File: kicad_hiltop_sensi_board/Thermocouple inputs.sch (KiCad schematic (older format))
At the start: 28 parts, among them U23 MAX4194, U24 MAX4194, U25 MAX4194, U26 MAX4194

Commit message: Updated board layout LBBC sensi board
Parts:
- R69: value R -> 100R 0.1%
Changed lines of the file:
@@
 	0    1    1    0
-$EndComp
-$Comp
-L Devtank:+3.3V #PWR0134
-U 1 1 5DE2BF89
-P 4500 1450
-F 0 "#PWR0134" H 4500 1300 50  0001 C CNN
-F 1 "+3.3V" H 4515 1623 50  0000 C CNN
-F 2 "" H 4500 1450 50  0000 C CNN
-F 3 "" H 4500 1450 50  0000 C CNN
-	1    4500 1450
-	1    0    0    -1
 $EndComp
 Connection ~ 4500 2600
@@
 	0    1    1    0
 $EndComp
-$Comp
-L Devtank:+3.3V #PWR0153
-U 1 1 5D86DCA3
-P 8300 1450
-F 0 "#PWR0153" H 8300 1300 50  0001 C CNN
-F 1 "+3.3V" H 8315 1623 50  0000 C CNN
-F 2 "" H 8300 1450 50  0000 C CNN
-F 3 "" H 8300 1450 50  0000 C CNN
-	1    8300 1450
-	1    0    0    -1
-$EndComp
 Connection ~ 8300 2600
 Wire Wire Line
@@
 	0    1    1    0
 $EndComp
-$Comp
-L Devtank:+3.3V #PWR0168
-U 1 1 5D874544
-P 4500 3850
-F 0 "#PWR0168" H 4500 3700 50  0001 C CNN
-F 1 "+3.3V" H 4515 4023 50  0000 C CNN
-F 2 "" H 4500 3850 50  0000 C CNN
-F 3 "" H 4500 3850 50  0000 C CNN
-	1    4500 3850
-	1    0    0    -1
-$EndComp
 Connection ~ 4500 5000
 Wire Wire Line
@@
 P 3850 4600
 F 0 "R69" H 3920 4646 50  0000 L CNN
-F 1 "R" H 3920 4555 50  0000 L CNN
+F 1 "100R 0.1%" H 3650 4450 50  0000 L CNN
 F 2 "Resistor_SMD:R_0603_1608Metric" V 3780 4600 50  0001 C CNN
 F 3 "" H 3850 4600 50  0001 C CNN
@@
 	0    1    1    0
 $EndComp
-$Comp
-L Devtank:+3.3V #PWR0173
-U 1 1 5D879C85
-P 8250 3800
-F 0 "#PWR0173" H 8250 3650 50  0001 C CNN
-F 1 "+3.3V" H 8265 3973 50  0000 C CNN
-F 2 "" H 8250 3800 50  0000 C CNN
-F 3 "" H 8250 3800 50  0000 C CNN
-	1    8250 3800
-	1    0    0    -1
-$EndComp
 Connection ~ 8250 4950
 Wire Wire Line
@@
 Wire Wire Line
 	6700 4750 7150 4750
+$Comp
+L power:+3V3 #PWR?
+U 1 1 5E6F1DC0
+P 4500 1450
+AR Path="/5E6F1DC0" Ref="#PWR?"  Part="1"
+AR Path="/5D6F87E7/5E6F1DC0" Ref="#PWR0247"  Part="1"
+F 0 "#PWR0247" H 4500 1300 50  0001 C CNN
+F 1 "+3V3" H 4515 1623 50  0000 C CNN
+F 2 "" H 4500 1450 50  0001 C CNN
+F 3 "" H 4500 1450 50  0001 C CNN
+	1    4500 1450
+	1    0    0    -1
+$EndComp
+$Comp
+L power:+3V3 #PWR?
+U 1 1 5E6F9A9C
+P 8300 1450
+AR Path="/5E6F9A9C" Ref="#PWR?"  Part="1"
+AR Path="/5D6F87E7/5E6F9A9C" Ref="#PWR0251"  Part="1"
+F 0 "#PWR0251" H 8300 1300 50  0001 C CNN
+F 1 "+3V3" H 8315 1623 50  0000 C CNN
+F 2 "" H 8300 1450 50  0001 C CNN
+F 3 "" H 8300 1450 50  0001 C CNN
+	1    8300 1450
+	1    0    0    -1
+$EndComp
+$Comp
+L power:+3V3 #PWR?
+U 1 1 5E702ADB
+P 4500 3850
+AR Path="/5E702ADB" Ref="#PWR?"  Part="1"
+AR Path="/5D6F87E7/5E702ADB" Ref="#PWR0259"  Part="1"
+F 0 "#PWR0259" H 4500 3700 50  0001 C CNN
+F 1 "+3V3" H 4515 4023 50  0000 C CNN
+F 2 "" H 4500 3850 50  0001 C CNN
+F 3 "" H 4500 3850 50  0001 C CNN
+	1    4500 3850
+	1    0    0    -1
+$EndComp
+$Comp
+L power:+3V3 #PWR?
+U 1 1 5E70B2B1
+P 8250 3800
+AR Path="/5E70B2B1" Ref="#PWR?"  Part="1"
+AR Path="/5D6F87E7/5E70B2B1" Ref="#PWR0260"  Part="1"
+F 0 "#PWR0260" H 8250 3650 50  0001 C CNN
+F 1 "+3V3" H 8265 3973 50  0000 C CNN
+F 2 "" H 8250 3800 50  0001 C CNN
+F 3 "" H 8250 3800 50  0001 C CNN
+	1    8250 3800
+	1    0    0    -1
+$EndComp
 $EndSCHEMATC

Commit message: Sensi board updated pin map
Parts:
- C68, C69, C86, C87: footprint Capacitor_SMD:C_0603_1608Metric -> Capacitor_SMD:C_0402_1005Metric
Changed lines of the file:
@@
 F 0 "C68" V 4548 1800 50  0000 C CNN
 F 1 "0.1uF" V 4639 1800 50  0000 C CNN
-F 2 "Capacitor_SMD:C_0603_1608Metric" H 4838 1650 50  0001 C CNN
+F 2 "Capacitor_SMD:C_0402_1005Metric" H 4838 1650 50  0001 C CNN
 F 3 "" H 4800 1800 50  0001 C CNN
 	1    4800 1800
@@
 F 0 "C87" V 8348 1800 50  0000 C CNN
 F 1 "0.1uF" V 8439 1800 50  0000 C CNN
-F 2 "Capacitor_SMD:C_0603_1608Metric" H 8638 1650 50  0001 C CNN
+F 2 "Capacitor_SMD:C_0402_1005Metric" H 8638 1650 50  0001 C CNN
 F 3 "" H 8600 1800 50  0001 C CNN
 	1    8600 1800
@@
 F 0 "C69" V 4548 4200 50  0000 C CNN
 F 1 "0.1uF" V 4639 4200 50  0000 C CNN
-F 2 "Capacitor_SMD:C_0603_1608Metric" H 4838 4050 50  0001 C CNN
+F 2 "Capacitor_SMD:C_0402_1005Metric" H 4838 4050 50  0001 C CNN
 F 3 "" H 4800 4200 50  0001 C CNN
 	1    4800 4200
@@
 F 0 "C86" V 8298 4150 50  0000 C CNN
 F 1 "0.1uF" V 8389 4150 50  0000 C CNN
-F 2 "Capacitor_SMD:C_0603_1608Metric" H 8588 4000 50  0001 C CNN
+F 2 "Capacitor_SMD:C_0402_1005Metric" H 8588 4000 50  0001 C CNN
 F 3 "" H 8550 4150 50  0001 C CNN
 	1    8550 4150

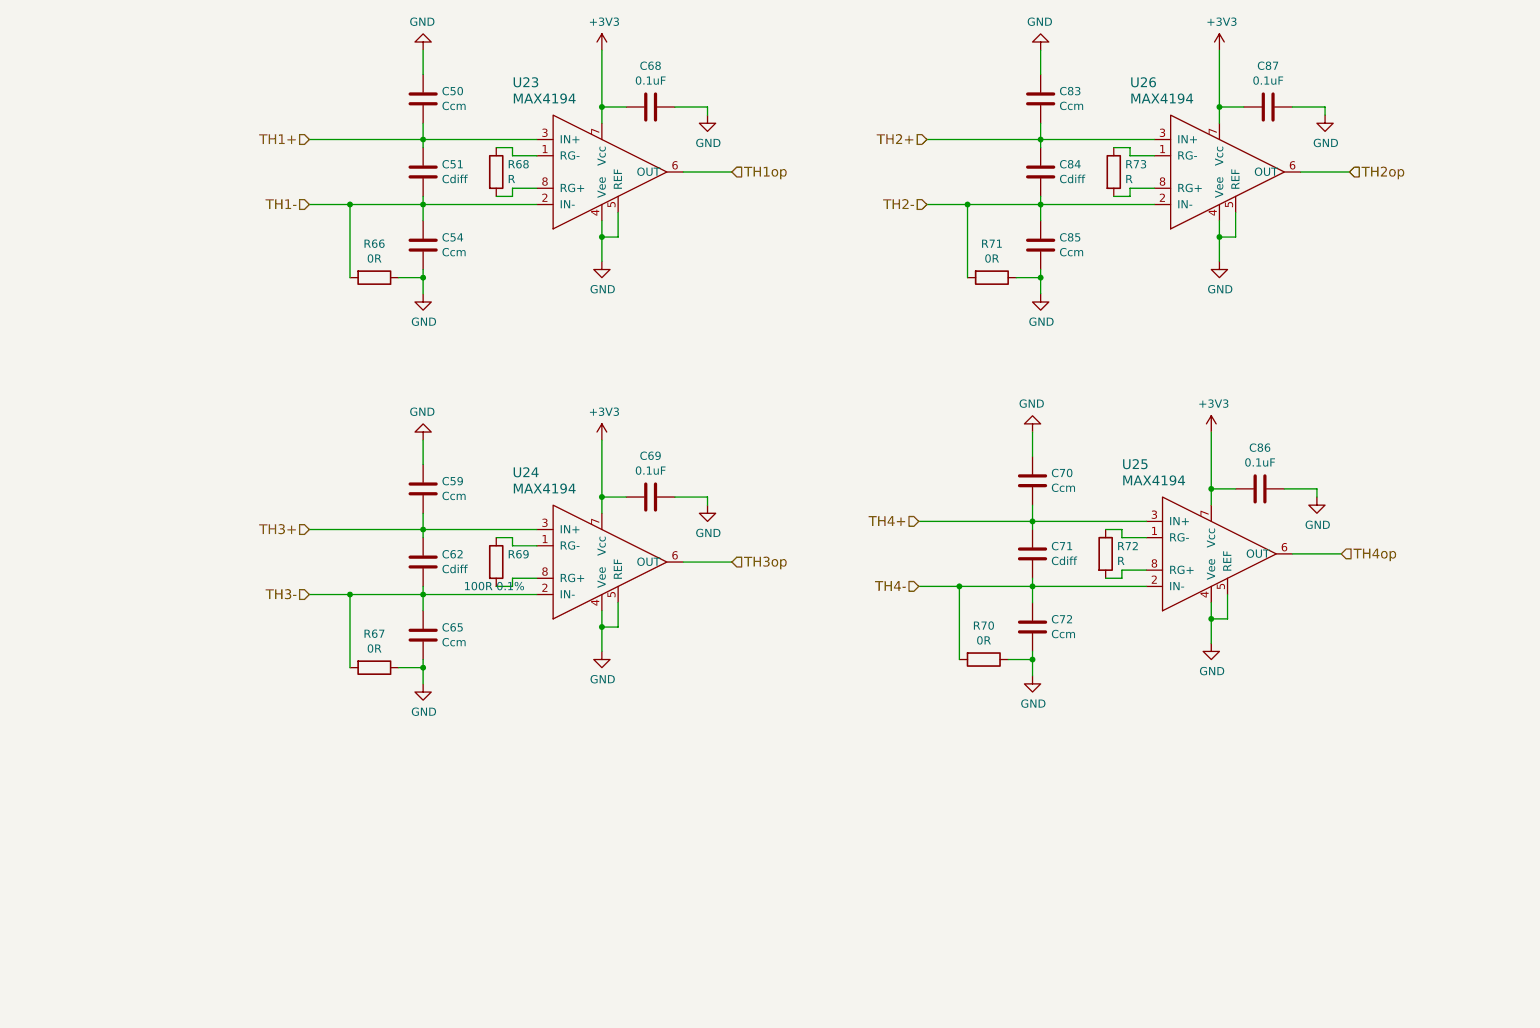
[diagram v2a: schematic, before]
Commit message: Updated sensi board pin map and layout before PCB tracking
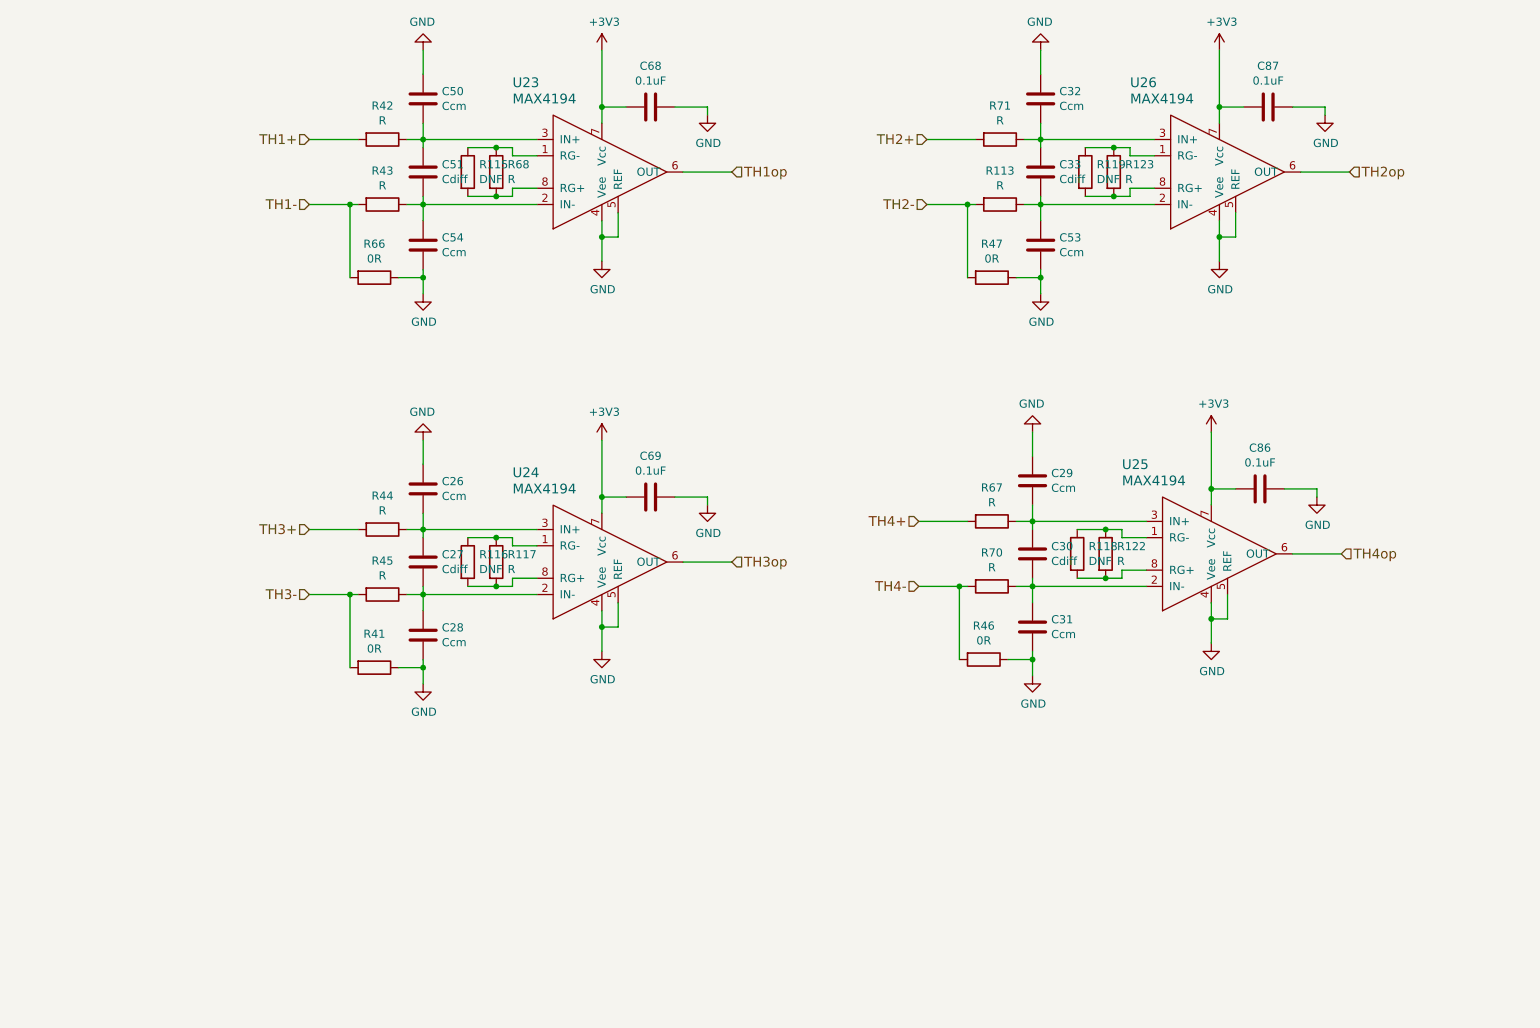
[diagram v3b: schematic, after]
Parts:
- removed C59, C65, C70, C72, C83, C85: Ccm, Capacitor_SMD:C_0603_1608Metric, symbol device:C
- removed C62, C71, C84: Cdiff, Capacitor_SMD:C_0603_1608Metric, symbol device:C
- removed R69: 100R 0.1%, Resistor_SMD:R_0603_1608Metric, symbol device:R
- removed R72, R73: R, Resistor_SMD:R_0603_1608Metric, symbol device:R
- added C26, C28, C29, C31, C32, C53: Ccm, Capacitor_SMD:C_0603_1608Metric, symbol device:C
- added C27, C30, C33: Cdiff, Capacitor_SMD:C_0603_1608Metric, symbol device:C
- added R113, R117, R122, R123, R42, R43, R44, R45: R, Resistor_SMD:R_0603_1608Metric, symbol device:R
- added R115, R116, R118, R119: DNF, Resistor_SMD:R_0603_1608Metric, symbol device:R
- added R41, R46, R47: 0R, Resistor_SMD:R_0603_1608Metric, symbol device:R
- C68, C69, C86, C87: Devtank (none) -> 105-019
- R66: Devtank (none) -> 101-005
- R67, R70, R71: value 0R -> R
- R68: Tolerance (none) -> 0.1%
- U23, U24, U25, U26: Devtank (none) -> 120-005
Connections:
- net GND: now also C26.1, C28.2, C29.1, C31.2, C32.1, C53.2, R41.1, R46.1, R47.1; no longer R67.1, R70.1, R71.1
- net TH1+: now also R42.2; no longer C50.2, C51.1, U23.3 (IN+)
- net TH1-: now also R43.2; no longer C51.2, C54.1, U23.2 (IN-)
- net TH2+: now also R71.2; no longer U26.3 (IN+)
- net TH2-: now also R113.2, R47.2; no longer R71.2, U26.2 (IN-)
- net TH3+: now also R44.2; no longer U24.3 (IN+)
- net TH3-: now also R41.2, R45.2; no longer R67.2, U24.2 (IN-)
- net TH4+: now also R67.2; no longer U25.3 (IN+)
- net TH4-: now also R46.2; no longer U25.2 (IN-)
- net at R68.1, U23.1 (RG-): now also R115.1
- net at R68.2, U23.8 (RG+): now also R115.2
- net at U26.1 (RG-): now also R119.1, R123.1
- net at U26.8 (RG+): now also R119.2, R123.2
- net at U24.1 (RG-): now also R116.1, R117.1
- net at U24.8 (RG+): now also R116.2, R117.2
- net at U25.1 (RG-): now also R118.1, R122.1
- net at U25.8 (RG+): now also R118.2, R122.2
- new net: C51.2, C54.1, R43.1, U23.2 (IN-)
- new net: C50.2, C51.1, R42.1, U23.3 (IN+)
- new net: C33.2, C53.1, R113.1, U26.2 (IN-)
- new net: C32.2, C33.1, R71.1, U26.3 (IN+)
- new net: C27.2, C28.1, R45.1, U24.2 (IN-)
- new net: C26.2, C27.1, R44.1, U24.3 (IN+)
- new net: C30.2, C31.1, R70.1, U25.2 (IN-)
- new net: C29.2, C30.1, R67.1, U25.3 (IN+)

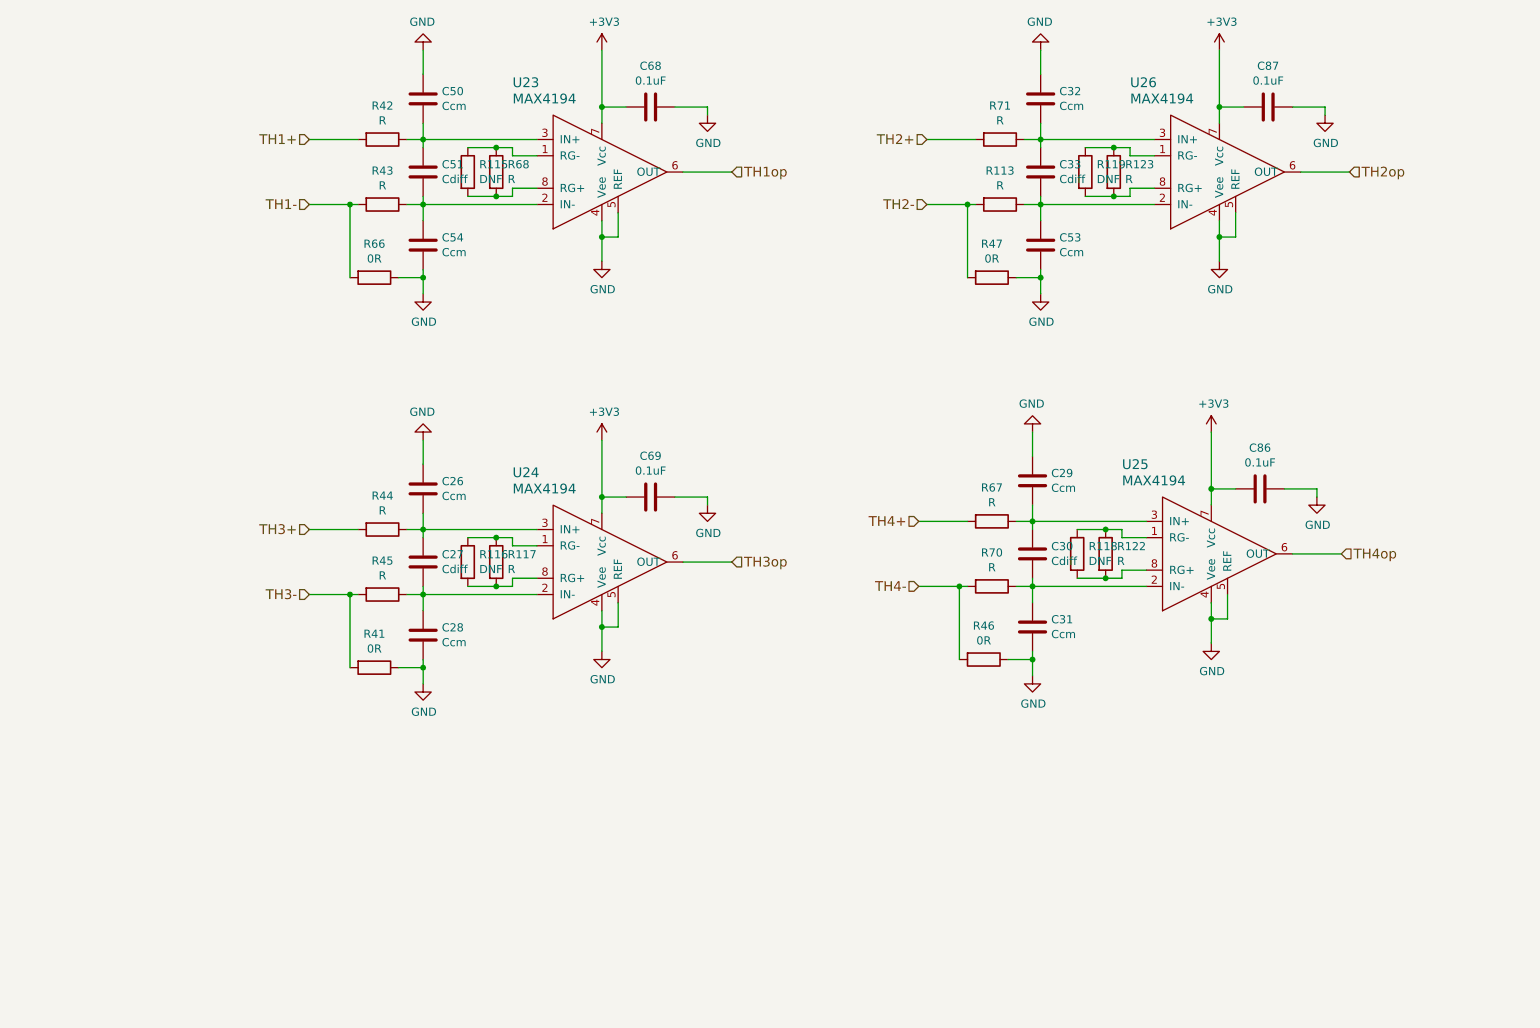
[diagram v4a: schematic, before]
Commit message: Changes to Sensi board after review
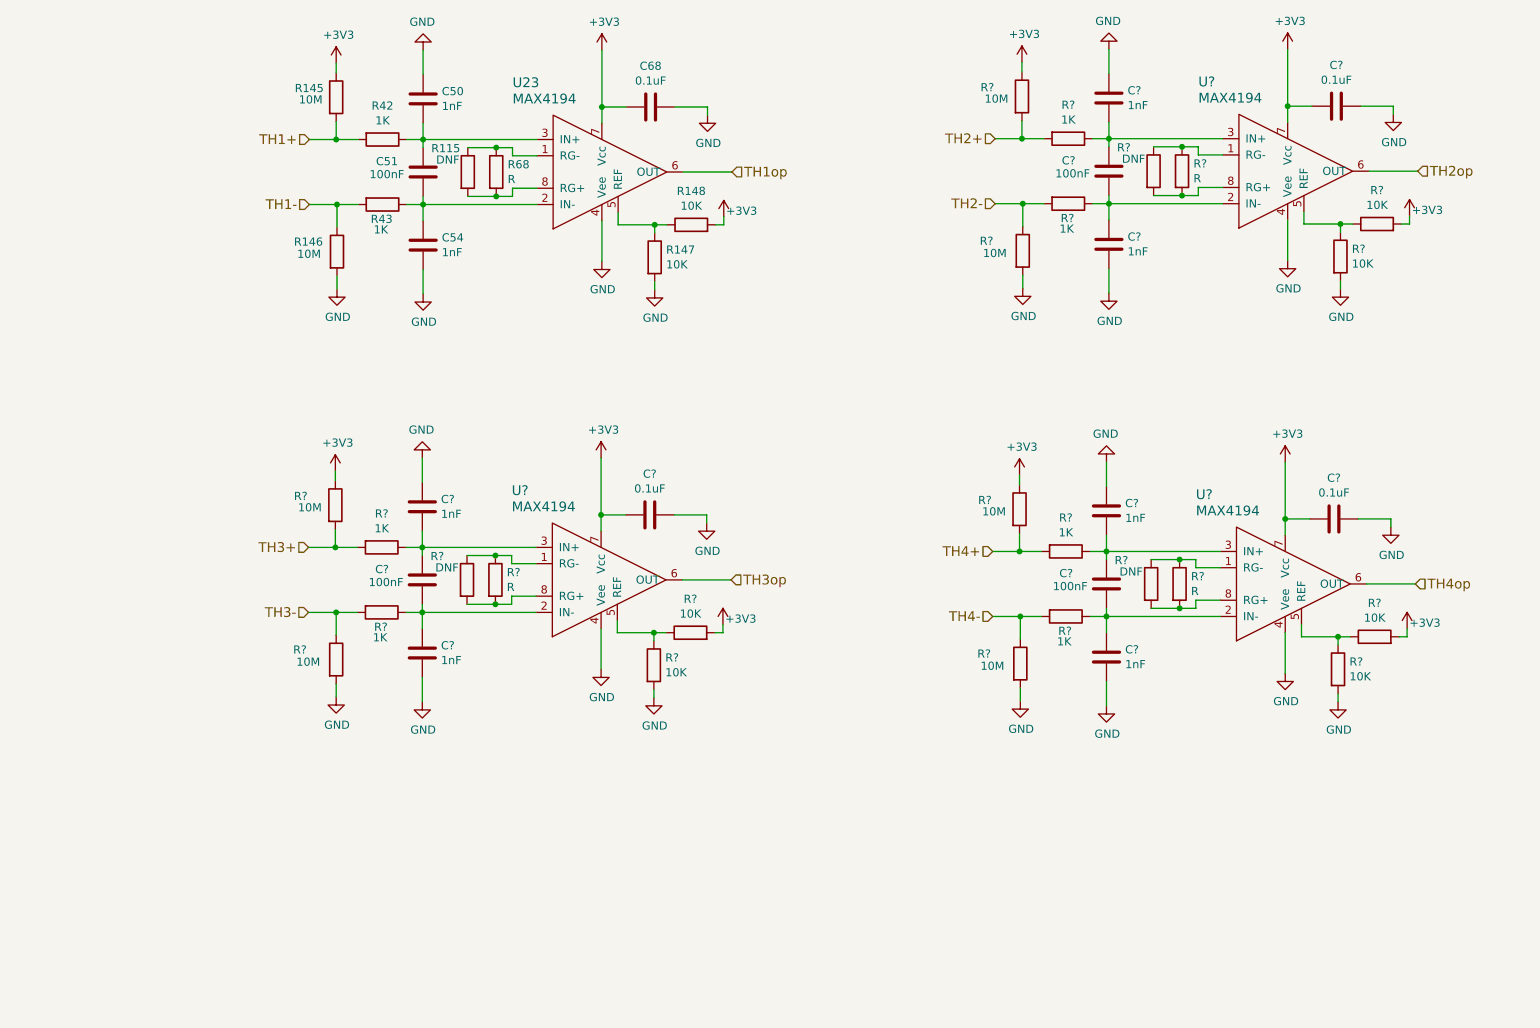
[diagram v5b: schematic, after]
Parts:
- removed C26, C28, C29, C31, C32, C53: Ccm, Capacitor_SMD:C_0603_1608Metric, symbol device:C
- removed C27, C30, C33: Cdiff, Capacitor_SMD:C_0603_1608Metric, symbol device:C
- removed C69, C86, C87: 0.1uF, Capacitor_SMD:C_0402_1005Metric, symbol device:C
- removed R113, R117, R122, R123, R44, R45, R67, R70, R71: R, Resistor_SMD:R_0603_1608Metric, symbol device:R
- removed R116, R118, R119: DNF, Resistor_SMD:R_0603_1608Metric, symbol device:R
- removed R41, R46, R47, R66: 0R, Resistor_SMD:R_0603_1608Metric, symbol device:R
- removed U24, U25, U26: MAX4194, Package_SO:SOIC-8_3.9x4.9mm_P1.27mm, symbol Sensi_Board-rescue:MAX4194-Devtank
- added C? (x6): 1nF, Capacitor_SMD:C_0603_1608Metric, symbol device:C
- added C? (x3): 100nF, Capacitor_SMD:C_0603_1608Metric, symbol device:C
- added C? (x3): 0.1uF, Capacitor_SMD:C_0402_1005Metric, symbol device:C
- added R145, R146, R? (x6): 10M, symbol device:R
- added R147, R148, R? (x6): 10K, symbol device:R
- added R? (x3): R, Resistor_SMD:R_0603_1608Metric, symbol device:R
- added R? (x6): 1K, Resistor_SMD:R_0603_1608Metric, symbol device:R
- added R? (x3): DNF, Resistor_SMD:R_0603_1608Metric, symbol device:R
- added U? (x3): MAX4194, Package_SO:SOIC-8_3.9x4.9mm_P1.27mm, symbol Sensi_Board-rescue:MAX4194-Devtank
- C50, C54: value Ccm -> 1nF
- C51: value Cdiff -> 100nF
- R42, R43: value R -> 1K
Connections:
- net +3V3: now also C?.2, C?.2, C?.2, R145.1, R148.2, R?.1, R?.1, R?.1, R?.2, R?.2, R?.2, U?.7 (Vcc), U?.7 (Vcc), U?.7 (Vcc)
- net GND: now also C?.1, C?.1, C?.1, C?.1, C?.1, C?.1, C?.2, C?.2, C?.2, R146.2, R147.2, R?.2, R?.2, R?.2, R?.2, R?.2, R?.2, U?.4 (Vee), U?.4 (Vee), U?.4 (Vee); no longer U23.5 (REF)
- net TH1+: now also R145.2
- net TH1-: now also R146.1
- net TH2+: now also R?.2, R?.2
- net TH2-: now also R?.1, R?.2
- net TH2op: now also U?.6 (OUT)
- net TH3+: now also R?.2, R?.2
- net TH3-: now also R?.1, R?.2
- net TH3op: now also U?.6 (OUT)
- net TH4+: now also R?.2, R?.2
- net TH4-: now also R?.1, R?.2
- net TH4op: now also U?.6 (OUT)
- new net: R147.1, R148.1, U23.5 (REF)
- new net: C?.1, C?.2, R?.1, U?.2 (IN-) (x3)
- new net: C?.1, C?.2, R?.1, U?.3 (IN+) (x3)
- new net: R?.1, R?.1, U?.1 (RG-) (x3)
- new net: R?.2, R?.2, U?.8 (RG+) (x3)
- new net: R?.1, R?.1, U?.5 (REF) (x3)
